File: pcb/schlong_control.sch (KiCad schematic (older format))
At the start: 26 parts

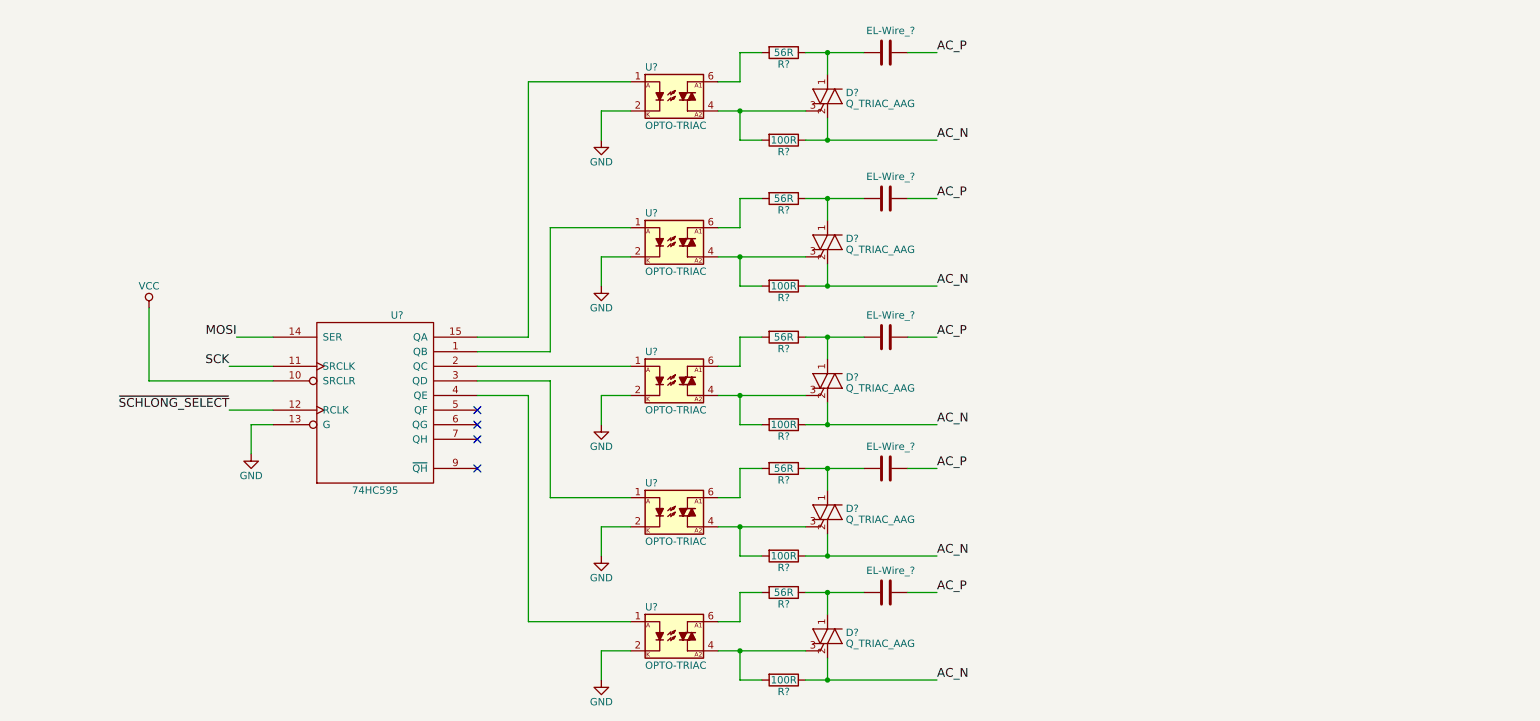
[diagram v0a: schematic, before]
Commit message: add data and power connectors / pass ERC
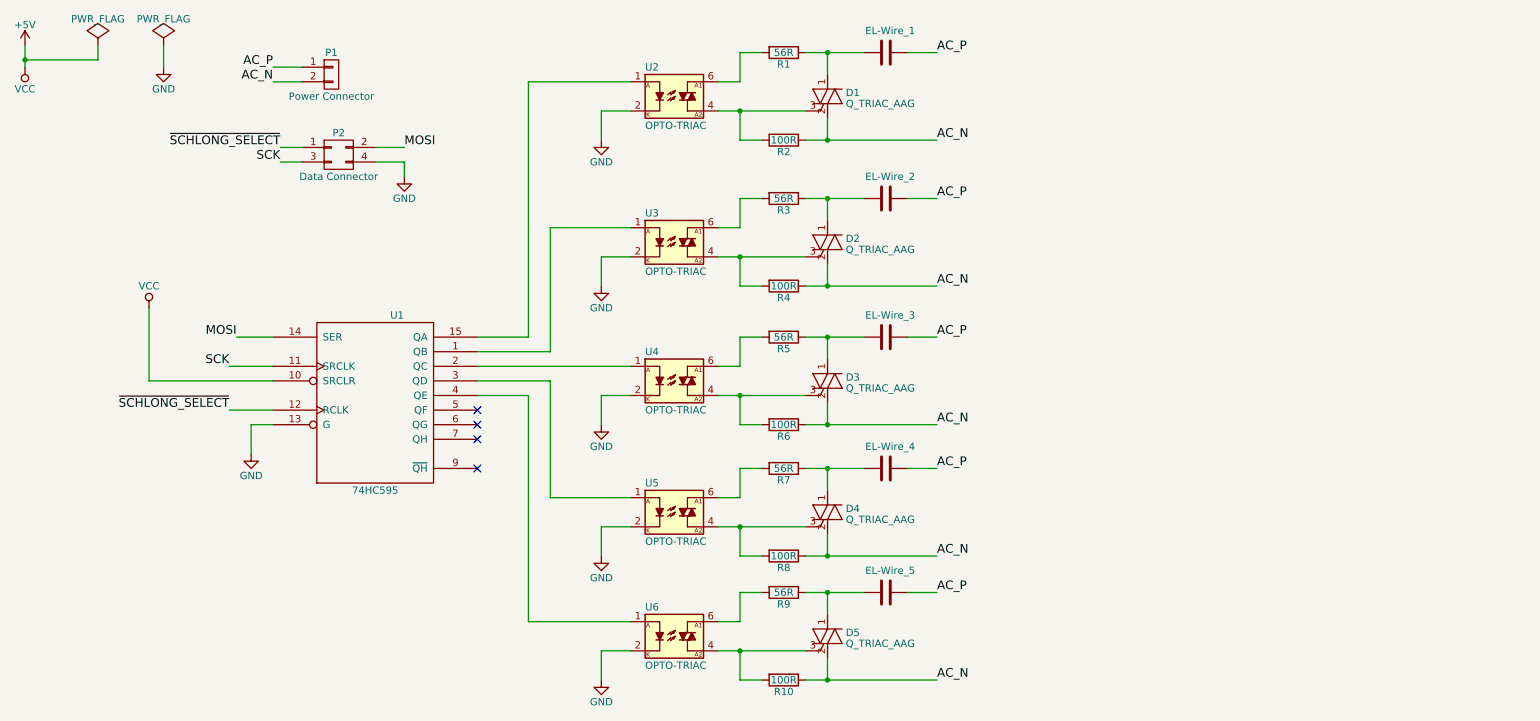
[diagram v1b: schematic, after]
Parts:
- added P1: Power Connector, symbol CONN_01X02
- added P2: Data Connector, symbol CONN_02X02
- gave numbers to parts that had none: 26
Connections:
- net AC_N: now also P1.2 (P2)
- net AC_P: now also P1.1 (P1)
- net GND: now also P2.4 (P4)
- net MOSI: now also P2.2 (P2)
- net SCK: now also P2.3 (P3)
- net ~SCHLONG_SELECT: now also P2.1 (P1)
- net VCC renamed +5V

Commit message: update circuit
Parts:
- removed R10, R2, R4, R6, R8: 100R, symbol R
- removed U2, U3, U4, U5, U6: OPTO-TRIAC, symbol OPTO-TRIAC
- added U2, U3, U4, U5, U6: MOC3063M, DIP-6, symbol MOC3063M
- R1: value 56R -> 4K7
- R2: renamed from R3; value 56R -> 4K7
- R3: renamed from R5; value 56R -> 4K7
- R4: renamed from R7; value 56R -> 4K7
- R5: renamed from R9; value 56R -> 4K7
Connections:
- net GND: now also U2.2, U3.2, U4.2, U5.2, U6.2
- net at U1.1 (QB): now also U3.1
- net at U1.15 (QA): now also U2.1
- net at U1.2 (QC): now also U4.1
- net at U1.3 (QD): now also U5.1
- net at U1.4 (QE): now also U6.1
- net at D1.3 (G): now also U2.4
- net at R1.2: now also U2.6
- net at D2.3 (G): now also U3.4
- net at R2.2: now also U3.6
- net at D3.3 (G): now also U4.4
- net at R3.2: now also U4.6
- net at D4.3 (G): now also U5.4
- net at R4.2: now also U5.6
- net at D5.3 (G): now also U6.4
- net at R5.2: now also U6.6

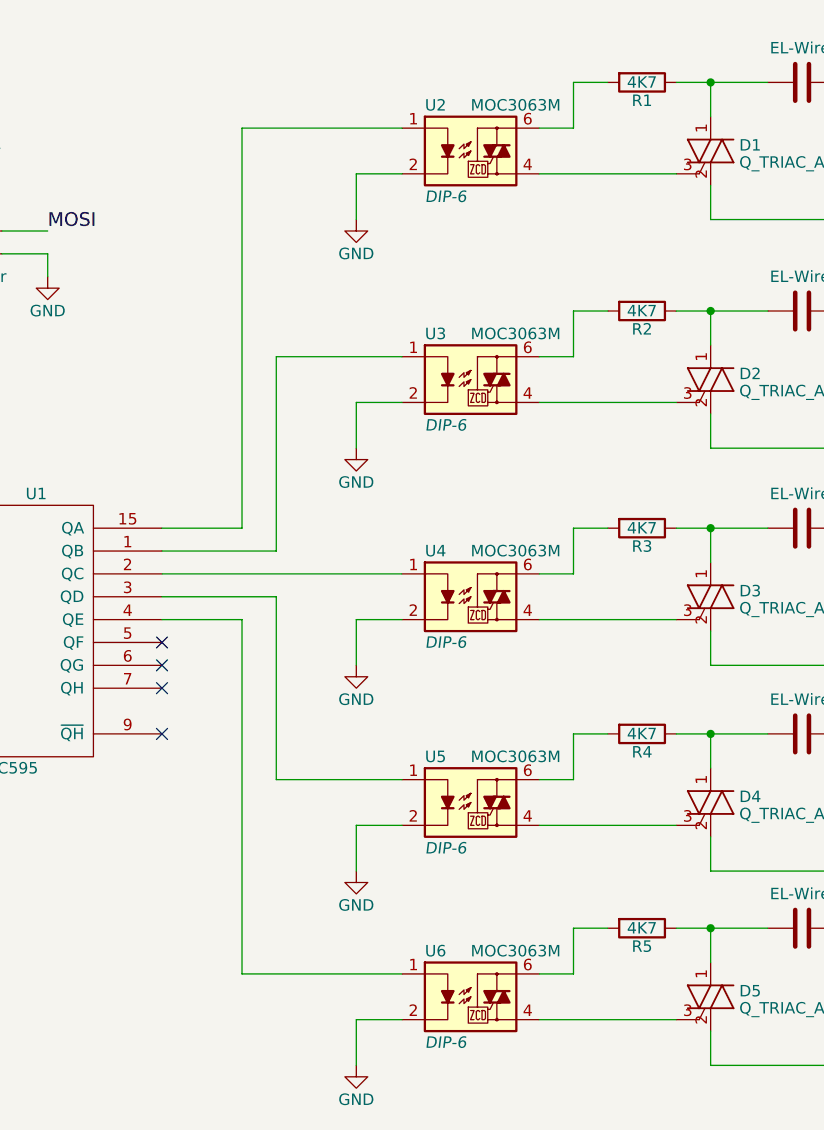
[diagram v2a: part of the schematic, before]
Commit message: add resistor to led of each opto triac
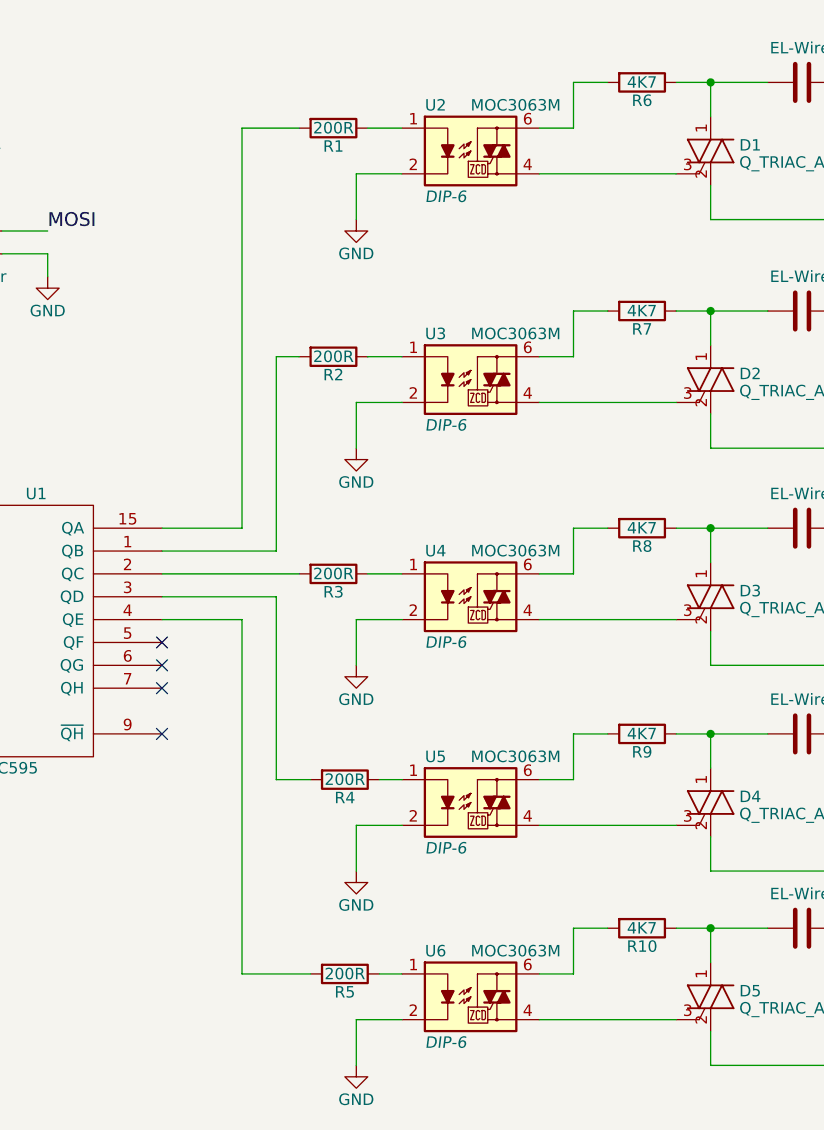
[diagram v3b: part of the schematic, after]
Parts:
- added R1, R2, R3, R4, R5: 200R, symbol R
- renumbered R5 to R10, R1 to R6, R2 to R7, R3 to R8, R4 to R9
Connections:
- net at U1.1 (QB): now also R2.2; no longer U3.1
- net at U1.15 (QA): now also R1.2; no longer U2.1
- net at U1.2 (QC): now also R3.2; no longer U4.1
- net at U1.3 (QD): now also R4.2; no longer U5.1
- net at U1.4 (QE): now also R5.2; no longer U6.1
- new net: R1.1, U2.1
- new net: R2.1, U3.1
- new net: R3.1, U4.1
- new net: R4.1, U5.1
- new net: R5.1, U6.1
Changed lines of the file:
@@
 $EndComp
 $Comp
-L R R1
+L R R6
 U 1 1 58A8C8E4
 P 6100 950
-F 0 "R1" V 6180 950 50  0000 C CNN
+F 0 "R6" V 6180 950 50  0000 C CNN
 F 1 "4K7" V 6100 950 50  0000 C CNN
 F 2 "" V 6030 950 50  0000 C CNN
@@
 $EndComp
 $Comp
-L R R2
+L R R7
 U 1 1 58A941A9
 P 6100 1950
-F 0 "R2" V 6180 1950 50  0000 C CNN
+F 0 "R7" V 6180 1950 50  0000 C CNN
 F 1 "4K7" V 6100 1950 50  0000 C CNN
 F 2 "" V 6030 1950 50  0000 C CNN
@@
 $EndComp
 $Comp
-L R R3
+L R R8
 U 1 1 58A94276
 P 6100 2900
-F 0 "R3" V 6180 2900 50  0000 C CNN
+F 0 "R8" V 6180 2900 50  0000 C CNN
 F 1 "4K7" V 6100 2900 50  0000 C CNN
 F 2 "" V 6030 2900 50  0000 C CNN
@@
 $EndComp
 $Comp
-L R R4
+L R R9
 U 1 1 58A94353
 P 6100 3800
-F 0 "R4" V 6180 3800 50  0000 C CNN
+F 0 "R9" V 6180 3800 50  0000 C CNN
 F 1 "4K7" V 6100 3800 50  0000 C CNN
 F 2 "" V 6030 3800 50  0000 C CNN
@@
 $EndComp
 $Comp
-L R R5
+L R R10
 U 1 1 58A94816
 P 6100 4650
-F 0 "R5" V 6180 4650 50  0000 C CNN
+F 0 "R10" V 6180 4650 50  0000 C CNN
 F 1 "4K7" V 6100 4650 50  0000 C CNN
 F 2 "" V 6030 4650 50  0000 C CNN
@@
 	4350 1150 4350 2900
 Wire Wire Line
-	4350 1150 5050 1150
-Wire Wire Line
 	6250 950  6650 950
 Wire Wire Line
@@
 	6950 4650 7150 4650
 Wire Wire Line
-	5050 2150 4500 2150
-Wire Wire Line
 	4500 2150 4500 3000
 Wire Wire Line
-	5050 3100 4000 3100
-Wire Wire Line
 	4350 2900 4000 2900
 Wire Wire Line
@@
 	4500 3200 4500 4000
 Wire Wire Line
-	4500 4000 5050 4000
-Wire Wire Line
 	4350 3300 4350 4850
 Wire Wire Line
 	4000 3300 4350 3300
-Wire Wire Line
-	4350 4850 5050 4850
 Wire Wire Line
 	2600 2900 2350 2900
@@
 	1    0    0    -1
 $EndComp
+$Comp
+L R R1
+U 1 1 58B4F0F1
+P 4750 1150
+F 0 "R1" V 4830 1150 50  0000 C CNN
+F 1 "200R" V 4750 1150 50  0000 C CNN
+F 2 "" V 4680 1150 50  0000 C CNN
+F 3 "" H 4750 1150 50  0000 C CNN
+	1    4750 1150
+	0    1    1    0
+$EndComp
+$Comp
+L R R2
+U 1 1 58B4F1FA
+P 4750 2150
+F 0 "R2" V 4830 2150 50  0000 C CNN
+F 1 "200R" V 4750 2150 50  0000 C CNN
+F 2 "" V 4680 2150 50  0000 C CNN
+F 3 "" H 4750 2150 50  0000 C CNN
+	1    4750 2150
+	0    1    1    0
+$EndComp
+$Comp
+L R R3
+U 1 1 58B4F255
+P 4750 3100
+F 0 "R3" V 4830 3100 50  0000 C CNN
+F 1 "200R" V 4750 3100 50  0000 C CNN
+F 2 "" V 4680 3100 50  0000 C CNN
+F 3 "" H 4750 3100 50  0000 C CNN
+	1    4750 3100
+	0    1    1    0
+$EndComp
+$Comp
+L R R4
+U 1 1 58B4F2B2
+P 4800 4000
+F 0 "R4" V 4880 4000 50  0000 C CNN
+F 1 "200R" V 4800 4000 50  0000 C CNN
+F 2 "" V 4730 4000 50  0000 C CNN
+F 3 "" H 4800 4000 50  0000 C CNN
+	1    4800 4000
+	0    1    1    0
+$EndComp
+$Comp
+L R R5
+U 1 1 58B4F305
+P 4800 4850
+F 0 "R5" V 4880 4850 50  0000 C CNN
+F 1 "200R" V 4800 4850 50  0000 C CNN
+F 2 "" V 4730 4850 50  0000 C CNN
+F 3 "" H 4800 4850 50  0000 C CNN
+	1    4800 4850
+	0    1    1    0
+$EndComp
+Wire Wire Line
+	4350 1150 4600 1150
+Wire Wire Line
+	4900 1150 5050 1150
+Wire Wire Line
+	4500 2150 4600 2150
+Wire Wire Line
+	4900 2150 5050 2150
+Wire Wire Line
+	4900 3100 5050 3100
+Wire Wire Line
+	4000 3100 4600 3100
+Wire Wire Line
+	4500 4000 4650 4000
+Wire Wire Line
+	4950 4000 5050 4000
+Wire Wire Line
+	4350 4850 4650 4850
+Wire Wire Line
+	4950 4850 5050 4850
 $EndSCHEMATC
